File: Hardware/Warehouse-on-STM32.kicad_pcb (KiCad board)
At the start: 2 copper layers, 456.6 x 276.9 mm, 73 parts, among them J1 ESP8266, J2 Conn_01x05, J3 Barrel_Jack_Switch, J4 Conn_01x02, J5 Conn_01x02, J6 Conn_01x02, Q1 AO3400A, Q2 AO3400A, SW1 SW_Push, SW2 SW_Push, SW3 SW_Push, SW4 SW_Push, U1 STM32F103C8Tx, U10 SGP30, U11 Sensor, U2 MP2225GJ, U3 AMS1117-1.8, U4 AMS1117-2.5, U5 AMS1117-3.3, U6 DRV8820DSG, U7 DRV8820DSG, U8 DRV8820DSG, U9 AHT20, Y1 Crystal

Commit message: nm
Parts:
- removed JP1, JP2: SolderJumper_3_Open, Jumper:SolderJumper-3_P2.0mm_Open_TrianglePad1.0x1.5mm
- removed U10: SGP30, My_Sensor:SGP30
- removed U11: Sensor, My_Sensor:MEMS气体传感器
- added L2: 1.5uH, Inductor_SMD:L_Chilisin_BMRA00050520, F.Cu at (60.4, 93.4)
- added L3: 1.5uH, Inductor_SMD:L_Chilisin_BMRA00050520, F.Cu at (53.5, 93.4)
- added L4: 4.7uH, Inductor_SMD:L_Chilisin_BMRA00050520, F.Cu at (67.0, 81.4)
- added R14: 40.2K, Resistor_SMD:R_0402_1005Metric, F.Cu at (56.2, 83.2)
- added R15: 5.49K, Resistor_SMD:R_0402_1005Metric, F.Cu at (53.2, 83.2)
- added R16: 4.7K, Resistor_SMD:R_0402_1005Metric, F.Cu at (67.7, 100.5)
- added R17: 4.7K, Resistor_SMD:R_0402_1005Metric, F.Cu at (69.0, 100.5)
- added R18: 4.7K, Resistor_SMD:R_0402_1005Metric, F.Cu at (51.0, 99.2)
- added R19: 1M, Resistor_SMD:R_0402_1005Metric, F.Cu at (60.2, 104.1)
- added R20: 4.7K, Resistor_SMD:R_0402_1005Metric, F.Cu at (56.3, 99.2)
- C10, C4: value 33pF -> 10uF
- C11: value 22uF -> 220pF; footprint Capacitor_SMD:C_1206_3216Metric -> Capacitor_SMD:C_0402_1005Metric
- C12, C13: value 10uF -> 220pF; footprint Capacitor_SMD:C_0603_1608Metric -> Capacitor_SMD:C_0402_1005Metric
- C14, C18: footprint Capacitor_SMD:C_0603_1608Metric -> Capacitor_SMD:C_0402_1005Metric
- C15: value 104 -> 1uF
- C16, C8, C9: value 104 -> 10uF
- C17, C23: value 104 -> 22uF; footprint Capacitor_SMD:C_0402_1005Metric -> Capacitor_SMD:C_0805_2012Metric
- C19, C20: value 10uF -> 104; footprint Capacitor_SMD:C_0603_1608Metric -> Capacitor_SMD:C_0402_1005Metric
- C22, C7: value 104 -> 33pF
- C24, C25, C26: footprint Capacitor_SMD:CP_Elec_4x5.4 -> Capacitor_SMD:C_0201_0603Metric
- C6: value 22uF -> 104; footprint Capacitor_SMD:C_1210_3225Metric -> Capacitor_SMD:C_0402_1005Metric
- L1: value 4.7uH -> 1.5uH; footprint Inductor_SMD:L_Chilisin_BMRx00060630 -> Inductor_SMD:L_Chilisin_BMRA00050520
- R10: value 4.7K -> 200K
- R11, R13: value 4.7K -> 100K
- R12: value 1M -> 100K
- R6: value 100K -> 510K
- R7: value 40.2K -> 110K
- R8: value 5.49K -> 470K
- R9: value 4.7K -> 150K
- U2: value MP2225GJ -> EA3036C; footprint Package_TO_SOT_SMD:TSOT-23-8 -> Package_DFN_QFN:QFN-20-1EP_3x3mm_P0.4mm_EP1.65x1.65mm
- U3: value AMS1117-1.8 -> MP2225GJ; footprint Package_TO_SOT_SMD:SOT-223-3_TabPin2 -> Package_TO_SOT_SMD:TSOT-23-8
- U4: value AMS1117-2.5 -> DRV8820DSG; footprint Package_TO_SOT_SMD:SOT-223-3_TabPin2 -> Package_SON:WSON-8-1EP_2x2mm_P0.5mm_EP0.9x1.6mm
- U5: value AMS1117-3.3 -> DRV8820DSG; footprint Package_TO_SOT_SMD:SOT-223-3_TabPin2 -> Package_SON:WSON-8-1EP_2x2mm_P0.5mm_EP0.9x1.6mm
- U7: value DRV8820DSG -> AHT20; footprint Package_SON:WSON-8-1EP_2x2mm_P0.5mm_EP0.9x1.6mm -> My_Sensor:AHT20
- U8: value DRV8820DSG -> SGP30; footprint Package_SON:WSON-8-1EP_2x2mm_P0.5mm_EP0.9x1.6mm -> My_Sensor:SGP30
- U9: value AHT20 -> Sensor; footprint My_Sensor:AHT20 -> My_Sensor:MEMS气体传感器
- moved C13 214.5 mm to (52.0, 86.8)
- moved C19 210.6 mm to (59.8, 79.1)
- moved C22 204.0 mm to (54.7, 83.2), turned to 90 degrees
- moved C16 200.3 mm to (54.8, 89.3), turned to 180 degrees
- moved C10 192.5 mm to (52.0, 89.3), turned to 0 degrees
- moved L1 190.9 mm to (67.0, 93.4), turned to 90 degrees
- moved R8 190.0 mm to (54.8, 86.8), turned to 0 degrees
- moved U2 188.4 mm to (60.1, 87.4), turned to 0 degrees
- moved C9 187.2 mm to (65.7, 89.3), turned to 0 degrees
- moved C12 184.2 mm to (54.8, 88.0)
- moved C11 182.5 mm to (68.5, 86.8)
- moved C18 177.7 mm to (57.8, 83.2), turned to 90 degrees
- moved R7 177.1 mm to (68.5, 85.5), turned to 180 degrees
- moved R6 177.0 mm to (68.5, 88.0), turned to 180 degrees
- moved C8 175.8 mm to (68.5, 89.3), turned to 180 degrees
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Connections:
- C10 pad 1: Net-(U2-FB) -> +1V8
- C10 pad 2: +5V -> GND
- C11 pad 1: +5V -> +3V3
- C11 pad 2: GND -> Net-(U2-FB1)
- C12 pad 1: +5V -> +2V5
- C12 pad 2: GND -> Net-(U2-FB2)
- C13 pad 1: +5V -> +1V8
- C13 pad 2: GND -> Net-(U2-LX3)
- C17 pad 1: +5V -> +12V
- C18 pad 1: +1V8 -> +5V
- C19 pad 1: +2V5 -> +12V
- C20 pad 1: +3V3 -> GND
- C20 pad 2: GND -> Net-(U3-VCC)
- C21 pad 1: +1V8 -> Net-(U3-BST)
- C21 pad 2: GND -> Net-(U3-SW)
- C22 pad 1: +2V5 -> +5V
- C22 pad 2: GND -> Net-(U3-FB)
- C23 pad 1: +3V3 -> +5V
- C4 pad 1: Net-(U1-PD0) -> +3V3
- C5 pad 1: Net-(U1-PD1) -> Net-(U1-PD0)
- C6 pad 1: +12V -> +3V3
- C7 pad 1: +12V -> Net-(U1-PD1)
- C8 pad 1: GND -> +3V3
- C8 pad 2: Net-(U2-VCC) -> GND
- C9 pad 1: Net-(U2-SW) -> +2V5
- C9 pad 2: Net-(U2-BST) -> GND
- L1 pad 1: Net-(U2-SW) -> +3V3
- L1 pad 2: +5V -> Net-(U2-LX1)
- R10 pad 1: +3V3 -> +1V8
- R10 pad 2: /SDA -> Net-(U2-LX3)
- R11 pad 1: +1V8 -> GND
- R11 pad 2: /传感器模块/SDA1V8 -> Net-(U2-LX3)
- R12 pad 1: /ADC -> +5V
- R12 pad 2: GND -> Net-(U2-EN1)
- R13 pad 1: +1V8 -> +12V
- R13 pad 2: /传感器模块/SCL1V8 -> Net-(U3-EN/SYNC)
- R6 pad 1: +12V -> +3V3
- R6 pad 2: Net-(U2-EN/SYNC) -> Net-(U2-FB1)
- R7 pad 1: +5V -> GND
- R7 pad 2: Net-(U2-FB) -> Net-(U2-FB1)
- R8 pad 1: Net-(U2-FB) -> +2V5
- R8 pad 2: GND -> Net-(U2-FB2)
- R9 pad 1: +3V3 -> GND
- R9 pad 2: /SCL -> Net-(U2-FB2)
- U1 pad 20: /BOOT1 -> GND
- U1 pad 44: /BOOT0 -> GND
- U2 pad 2: +12V -> Net-(U2-FB3)
- U2 pad 3: Net-(U2-SW) -> Net-(U2-FB2)
- U2 pad 5: Net-(U2-BST) -> GND
- U2 pad 6: Net-(U2-EN/SYNC) -> Net-(U2-LX2)
- U2 pad 7: Net-(U2-VCC) -> +5V
- U2 pad 8: Net-(U2-FB) -> Net-(U2-EN1)
- U3 pad 2: +1V8 -> +12V
- U3 pad 3: +5V -> Net-(U3-SW)
- U4 pad 1: GND -> +12V
- U4 pad 2: +2V5 -> Net-(J4-Pin_1)
- U4 pad 3: +5V -> Net-(J4-Pin_2)
- U5 pad 1: GND -> +12V
- U5 pad 2: +3V3 -> Net-(J5-Pin_1)
- U5 pad 3: +5V -> Net-(J5-Pin_2)
- U6 pad 2: Net-(J4-Pin_1) -> Net-(J6-Pin_1)
- U6 pad 3: Net-(J4-Pin_2) -> Net-(J6-Pin_2)
- U6 pad 5: /AEN -> /CEN
- U6 pad 6: /APH -> +3V3
- U6 pad 8: /ASLEEP -> /CSLEEP
- U7 pad 1: +12V -> unconnected-(U7-NC-Pad1)
- U7 pad 2: Net-(J5-Pin_1) -> +3V3
- U7 pad 3: Net-(J5-Pin_2) -> /SCL
- U7 pad 4: GND -> /SDA
- U7 pad 5: /BEN -> GND
- U7 pad 6: +3V3 -> unconnected-(U7-NC-Pad6)
- U8 pad 1: +12V -> +1V8
- U8 pad 2: Net-(J6-Pin_1) -> GND
- U8 pad 3: Net-(J6-Pin_2) -> /传感器模块/SDA1V8
- U8 pad 5: /CEN -> +1V8
- U8 pad 6: +3V3 -> /传感器模块/SCL1V8
- U8 pad 7: +3V3 -> GND
- U9 pad 1: unconnected-(U9-NC-Pad1) -> +2V5
- U9 pad 2: +3V3 -> /ADC
- U9 pad 3: /SCL -> GND
- U9 pad 4: /SDA -> +3V3
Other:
- board size 456.6 x 276.9 mm -> 57 x 47 mm

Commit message: nm
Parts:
- J3: footprint Connector_BarrelJack:BarrelJack_CLIFF_FC681465S_SMT_Horizontal -> Connector_BarrelJack:BarrelJack_XKB_DC-044A-2.5A-2.5
- moved J3 3.98 mm to (64.7, 65.3), turned to 0 degrees
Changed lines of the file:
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@@
     )
   )
-  (footprint "Connector_BarrelJack:BarrelJack_CLIFF_FC681465S_SMT_Horizontal" (layer "F.Cu")
-    (at 65.19 69.294 -90)
-    (descr "Surface-mount DC Barrel Jack, https://www.cliffuk.co.uk/products/dcconnectors/FC681465S.pdf")
-    (tags "Power Jack SMT")
+  (footprint "Connector_BarrelJack:BarrelJack_XKB_DC-044A-2.5A-2.5" (layer "F.Cu")
+    (at 64.7 65.346)
     (property "Sheetfile" "电源模块.kicad_sch")
     (property "Sheetname" "电源模块")
@@
     (property "ki_keywords" "DC power barrel jack connector")
     (attr smd)
-    (fp_text reference "J3" (at -6.5 6.5 90) (layer "F.SilkS") hide
+    (fp_text reference "J3" (at 0 -6.096 unlocked) (layer "F.SilkS")
+        (effects (font (size 1 1) (thickness 0.1)))
+    )
+    (fp_text value "Barrel_Jack_Switch" (at 0 8.128 unlocked) (layer "F.Fab")
         (effects (font (size 1 1) (thickness 0.15)))
     )
-    (fp_text value "Barrel_Jack_Switch" (at -0.5 8.5 90) (layer "F.Fab")
+    (fp_text user "${REFERENCE}" (at -0.127 9.779 unlocked) (layer "F.Fab")
         (effects (font (size 1 1) (thickness 0.15)))
     )
-    (fp_text user "${REFERENCE}" (at -0.5 0.5 90) (layer "F.Fab")
-        (effects (font (size 1 1) (thickness 0.15)))
-    )
-    (fp_line (start -8.11 -4.56) (end -4.5 -4.56)
-      (stroke (width 0.12) (type solid)) (layer "F.SilkS"))
-    (fp_line (start -8.11 4.56) (end -8.11 -4.56)
-      (stroke (width 0.12) (type solid)) (layer "F.SilkS"))
-    (fp_line (start -8.11 4.56) (end -4.5 4.56)
-      (stroke (width 0.12) (type solid)) (layer "F.SilkS"))
-    (fp_line (start -4.8 -3) (end 0 -3)
-      (stroke (width 0.12) (type solid)) (layer "F.SilkS"))
-    (fp_line (start -4.8 3) (end 0 3)
-      (stroke (width 0.12) (type solid)) (layer "F.SilkS"))
-    (fp_line (start -4.8 4.56) (end -4.8 -4.56)
-      (stroke (width 0.12) (type solid)) (layer "F.SilkS"))
-    (fp_line (start -4.26 -7.26) (end -4.26 -5.36)
-      (stroke (width 0.12) (type solid)) (layer "F.SilkS"))
-    (fp_line (start -2.92 -7.26) (end -4.26 -7.26)
-      (stroke (width 0.12) (type solid)) (layer "F.SilkS"))
-    (fp_line (start -1.5 -4.56) (end 1.5 -4.56)
-      (stroke (width 0.12) (type solid)) (layer "F.SilkS"))
-    (fp_line (start -1.5 4.56) (end 1.5 4.56)
-      (stroke (width 0.12) (type solid)) (layer "F.SilkS"))
-    (fp_line (start 4.5 -4.56) (end 6.81 -4.56)
-      (stroke (width 0.12) (type solid)) (layer "F.SilkS"))
-    (fp_line (start 4.5 4.56) (end 6.81 4.56)
-      (stroke (width 0.12) (type solid)) (layer "F.SilkS"))
-    (fp_line (start 6.81 4.56) (end 6.81 -4.56)
-      (stroke (width 0.12) (type solid)) (layer "F.SilkS"))
-    (fp_arc (start 0 -3) (mid 3 0) (end 0 3)
-      (stroke (width 0.12) (type solid)) (layer "F.SilkS"))
-    (fp_line (start -8.5 -7.5) (end 7.2 -7.5)
-      (stroke (width 0.05) (type solid)) (layer "F.CrtYd"))
-    (fp_line (start -8.5 7.5) (end -8.5 -7.5)
-      (stroke (width 0.05) (type solid)) (layer "F.CrtYd"))
-    (fp_line (start -8.5 7.5) (end 7.2 7.5)
-      (stroke (width 0.05) (type solid)) (layer "F.CrtYd"))
-    (fp_line (start 7.2 7.5) (end 7.2 -7.5)
-      (stroke (width 0.05) (type solid)) (layer "F.CrtYd"))
-    (fp_line (start -8 -4.45) (end -4 -4.45)
-      (stroke (width 0.1) (type solid)) (layer "F.Fab"))
-    (fp_line (start -8 4.45) (end -8 -4.45)
-      (stroke (width 0.1) (type solid)) (layer "F.Fab"))
-    (fp_line (start -8 4.45) (end 6.7 4.45)
-      (stroke (width 0.1) (type solid)) (layer "F.Fab"))
-    (fp_line (start -4 -4.45) (end -3 -3.5)
-      (stroke (width 0.1) (type solid)) (layer "F.Fab"))
-    (fp_line (start -3 -3.5) (end -2 -4.45)
-      (stroke (width 0.1) (type solid)) (layer "F.Fab"))
-    (fp_line (start -2 -4.45) (end 6.7 -4.45)
-      (stroke (width 0.1) (type solid)) (layer "F.Fab"))
-    (fp_line (start 6.7 4.45) (end 6.7 -4.45)
-      (stroke (width 0.1) (type solid)) (layer "F.Fab"))
-    (pad "" np_thru_hole oval (at -2.9 0) (size 2 1.5) (drill oval 2 1.5) (layers "*.Cu" "*.Mask"))
-    (pad "" np_thru_hole circle (at 1.5 0) (size 2 2) (drill 2) (layers "*.Cu" "*.Mask"))
-    (pad "1" smd rect (at -3 -5.5) (size 3 2) (layers "F.Cu" "F.Paste" "F.Mask")
-      (net 22 "Net-(J3-Pad1)") (pintype "passive"))
-    (pad "1" smd rect (at 3 -5.5) (size 3 2) (layers "F.Cu" "F.Paste" "F.Mask")
-      (net 22 "Net-(J3-Pad1)") (pintype "passive"))
-    (pad "2" smd rect (at 3 5.5) (size 3 2) (layers "F.Cu" "F.Paste" "F.Mask")
-      (net 2 "GND") (pintype "passive"))
-    (pad "3" smd rect (at -3 5.5) (size 3 2) (layers "F.Cu" "F.Paste" "F.Mask")
-      (net 2 "GND") (pintype "passive"))
-    (model "${KICAD6_3DMODEL_DIR}/Connector_BarrelJack.3dshapes/BarrelJack_CLIFF_FC681465S_SMT_Horizontal.wrl"
-      (offset (xyz 0 0 0))
+    (fp_line (start -4.75 -5.1) (end -4.75 -3.449)
+      (stroke (width 0.1) (type default)) (layer "F.SilkS"))
+    (fp_line (start -4.75 -5.1) (end 5.25 -5.1)
+      (stroke (width 0.1) (type default)) (layer "F.SilkS"))
+    (fp_line (start -4.75 -0.782) (end -4.75 4.298)
+      (stroke (width 0.1) (type default)) (layer "F.SilkS"))
+    (fp_line (start -4.75 6.75) (end -4.75 6.584)
+      (stroke (width 0.1) (type default)) (layer "F.SilkS"))
+    (fp_line (start 5.25 -5.1) (end 5.25 -3.449)
+      (stroke (width 0.1) (type default)) (layer "F.SilkS"))
+    (fp_line (start 5.25 6.75) (end -4.75 6.75)
+      (stroke (width 0.1) (type default)) (layer "F.SilkS"))
+    (fp_line (start 5.25 6.75) (end 5.25 -0.782)
+      (stroke (width 0.1) (type default)) (layer "F.SilkS"))
+    (fp_rect (start -2 -2) (end 0 0)
+      (stroke (width 0.1) (type default)) (fill none) (layer "Edge.Cuts"))
+    (pad "2" thru_hole oval (at 3.95 5.4 90) (size 2 1.1) (drill oval 1.6 0.8) (layers "*.Cu" "*.Mask")
+      (net 2 "GND") (pintype "passive") (solder_mask_margin 0.04) (thermal_bridge_angle 45))
+    (pad "3" thru_hole oval (at -1.25 5.4 90) (size 2 1.1) (drill oval 1.6 0.8) (layers "*.Cu" "*.Mask")
+      (net 2 "GND") (pintype "passive") (solder_mask_margin 0.04) (thermal_bridge_angle 45))
+    (pad "4" thru_hole oval (at -4.65 5.4 90) (size 2 1.1) (drill oval 1.6 0.8) (layers "*.Cu" "*.Mask")
+      (solder_mask_margin 0.04) (thermal_bridge_angle 45))
+    (pad "5" thru_hole oval (at -4.65 -2.1 90) (size 2.4 0.8) (drill oval 2 0.5) (layers "*.Cu" "*.Mask")
+      (solder_mask_margin 0.04) (thermal_bridge_angle 45))
+    (pad "5" thru_hole oval (at 5.15 -2.1 90) (size 2.4 0.8) (drill oval 2 0.5) (layers "*.Cu" "*.Mask")
+      (solder_mask_margin 0.04) (thermal_bridge_angle 45))
+    (model "${KICAD7_3DMODEL_DIR}/Connector_BarrelJack.3dshapes/BarellJack_XKB_DC-044A-2.5A-2.5.stp"
+      (offset (xyz 0.2 4.9 4))
       (scale (xyz 1 1 1))
-      (rotate (xyz 0 0 0))
+      (rotate (xyz 90 180 0))
     )
   )

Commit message: 完成布局
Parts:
- C1: footprint Capacitor_SMD:C_0603_1608Metric -> Capacitor_SMD:C_0402_1005Metric
- J2: footprint Connector_PinHeader_2.54mm:PinHeader_1x05_P2.54mm_Vertical -> Connector_PinHeader_1.00mm:PinHeader_1x05_P1.00mm_Vertical
- J3: value Barrel_Jack_Switch -> Barrel_Jack_Switch_MountingPin
- L1, L2, L3, L4: footprint Inductor_SMD:L_Chilisin_BMRA00050520 -> Inductor_SMD:L_1206_3216Metric
- SW1, SW2, SW3, SW4: footprint Button_Switch_SMD:SW_Tactile_SPST_NO_Straight_CK_PTS636Sx25SMTRLFS -> Button_Switch_SMD:SW_XKB_TS-1185-B-A-B-A
- SW5: footprint Library:SW -> Button_Switch_THT:SW_XKB_SS-12D10L5
- U7: footprint My_Sensor:AHT20 -> Sensor:AHT20
- U8: footprint My_Sensor:SGP30 -> Sensor:SGP30
- U9: footprint My_Sensor:MEMS气体传感器 -> Sensor:MEMS气体传感器
- Y1: value Crystal -> 8MHz; footprint Crystal:Crystal_SMD_5032-2Pin_5.0x3.2mm -> Crystal:Crystal_SMD_3225-4Pin_3.2x2.5mm
- moved SW5 75.8 mm to (119.4, 104.5), turned to 0 degrees
- moved R13 74.7 mm to (125.4, 112.7), turned to -90 degrees
- moved C20 74.6 mm to (119.4, 114.5), turned to 0 degrees
- moved C22 73.8 mm to (121.6, 114.5), turned to 180 degrees
- moved R15 73.8 mm to (119.4, 115.9), turned to 180 degrees
- moved R14 73.1 mm to (121.6, 115.9), turned to 180 degrees
- moved C19 72.7 mm to (125.4, 110.5), turned to 90 degrees
- moved U3 72.6 mm to (120.2, 111.5), turned to -90 degrees
- moved C21 71.9 mm to (116.8, 111.4)
- moved C17 69.8 mm to (123.4, 111.3), turned to -90 degrees
- moved Q2 67.5 mm to (113.2, 131.7)
- moved J2 66.1 mm to (149.8, 132.8), turned to -90 degrees
- moved C24 65.9 mm to (133.4, 110.6)
- moved C27 65.9 mm to (132.2, 110.8)
- moved C25 65.6 mm to (142.4, 110.6)
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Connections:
- C13 pad 2: Net-(U2-LX3) -> Net-(U2-FB3)
- J2 pad 1: /SWDIO -> /SWCLK
- J2 pad 2: /SWCLK -> /SWDIO
- J2 pad 4: /USART1_TX -> /USART1_RX
- J2 pad 5: /USART1_RX -> /USART1_TX
- L3 pad 2: Net-(U2-FB3) -> Net-(U2-LX3)
- R10 pad 2: Net-(U2-LX3) -> Net-(U2-FB3)
- R11 pad 2: Net-(U2-LX3) -> Net-(U2-FB3)
- U1 pad 14: unconnected-(U1-PA4-Pad14) -> /KEY2
- U1 pad 15: unconnected-(U1-PA5-Pad15) -> /KEY1
- U1 pad 16: /ASLEEP -> /KEY0
- U1 pad 17: /APH -> unconnected-(U1-PA7-Pad17)
- U1 pad 2: /KEY0 -> /ASLEEP
- U1 pad 21: /USART1_RX -> unconnected-(U1-PB10-Pad21)
- U1 pad 29: /AEN -> unconnected-(U1-PA8-Pad29)
- U1 pad 3: /KEY1 -> /APH
- U1 pad 30: /BSLEEP -> /USART1_TX
- U1 pad 31: /BEN -> /USART1_RX
- U1 pad 32: /CSLEEP -> unconnected-(U1-PA11-Pad32)
- U1 pad 33: /CEN -> unconnected-(U1-PA12-Pad33)
- U1 pad 38: unconnected-(U1-PA15-Pad38) -> /CSLEEP
- U1 pad 39: unconnected-(U1-PB3-Pad39) -> /CEN
- U1 pad 4: /KEY2 -> /AEN
- U1 pad 40: unconnected-(U1-PB4-Pad40) -> /BSLEEP
- U1 pad 41: unconnected-(U1-PB5-Pad41) -> /BEN
- U1 pad 46: /USART1_TX -> unconnected-(U1-PB9-Pad46)
- Y1 pad 2: Net-(U1-PD1) -> GND
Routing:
- added copper zone on F.Cu, net +12V
- added copper zone on B.Cu, net Net-(J3-Pad1)
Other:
- board size 57 x 47 mm -> 53 x 35 mm

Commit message: 完成部分布线
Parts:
- moved C18 0.80 mm to (107.8, 114.4)
- moved R12 0.40 mm to (109.6, 114.4)
- turned C19 to -90 degrees
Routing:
- net +1V8: track 0.00 -> 23.7 mm
- net +12V: track 0.00 -> 23.4 mm, vias 0 -> 12
- net +5V: track 0.00 -> 21.3 mm, vias 0 -> 6
- net Net-(U3-SW): track 0.00 -> 11.4 mm
- net Net-(U2-FB2): track 0.00 -> 10.9 mm
- net Net-(U2-FB1): track 0.00 -> 10.5 mm
- net Net-(U2-LX3): track 0.00 -> 10.0 mm
- net Net-(U2-EN1): track 0.00 -> 9.32 mm, vias 0 -> 2
- net Net-(U3-EN/SYNC): track 0.00 -> 6.73 mm, vias 0 -> 2
- net Net-(U2-FB3): track 0.00 -> 6.52 mm
- net Net-(J6-Pin_1): track 0.00 -> 5.97 mm
- net Net-(J5-Pin_1): track 0.00 -> 5.97 mm
- net Net-(J4-Pin_1): track 0.00 -> 5.97 mm
- net +3V3: track 0.00 -> 5.41 mm
- net +2V5: track 0.00 -> 5.41 mm
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- added copper zone on B.Cu, net +12V
- added copper zone on B.Cu, net +5V
- removed copper zone on F.Cu, net +12V

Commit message: 绘制第一版
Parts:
- moved R16 0.10 mm to (108.2, 126.9)
- moved R17 0.10 mm to (113.0, 126.9)
- moved C1 0.09 mm to (149.1, 114.6)
- moved R1 0.09 mm to (149.1, 115.8)
- turned R20 to 0 degrees
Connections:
- U1 pad 21: unconnected-(U1-PB10-Pad21) -> /SCL
- U1 pad 22: unconnected-(U1-PB11-Pad22) -> /SDA
- U1 pad 42: /SCL -> unconnected-(U1-PB6-Pad42)
- U1 pad 43: /SDA -> unconnected-(U1-PB7-Pad43)
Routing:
- net +3V3: track 5.41 -> 127.6 mm, vias 0 -> 14
- net /SCL: track 0.00 -> 38.3 mm, vias 0 -> 3
- net /SDA: track 0.00 -> 34.8 mm, vias 0 -> 4
- net /SWCLK: track 0.00 -> 24.2 mm
- net /ESP_TX: track 0.00 -> 23.3 mm, vias 0 -> 1
- net /ADC: track 0.00 -> 22.8 mm, vias 0 -> 4
- net /SWDIO: track 0.00 -> 19.6 mm
- net /ESP_RX: track 0.00 -> 19.5 mm, vias 0 -> 1
- net /USART1_RX: track 0.00 -> 17.2 mm
- net /USART1_TX: track 0.00 -> 16.2 mm
- net +1V8: track 23.7 -> 39.8 mm, vias 0 -> 2
- net +2V5: track 5.41 -> 21.3 mm
- net /CSLEEP: track 0.00 -> 14.0 mm
- net /传感器模块/SDA1V8: track 0.00 -> 13.6 mm, vias 0 -> 4
- net /CEN: track 0.00 -> 13.1 mm
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- added copper zone on B.Cu, net GND
- added copper zone on F.Cu, net GND

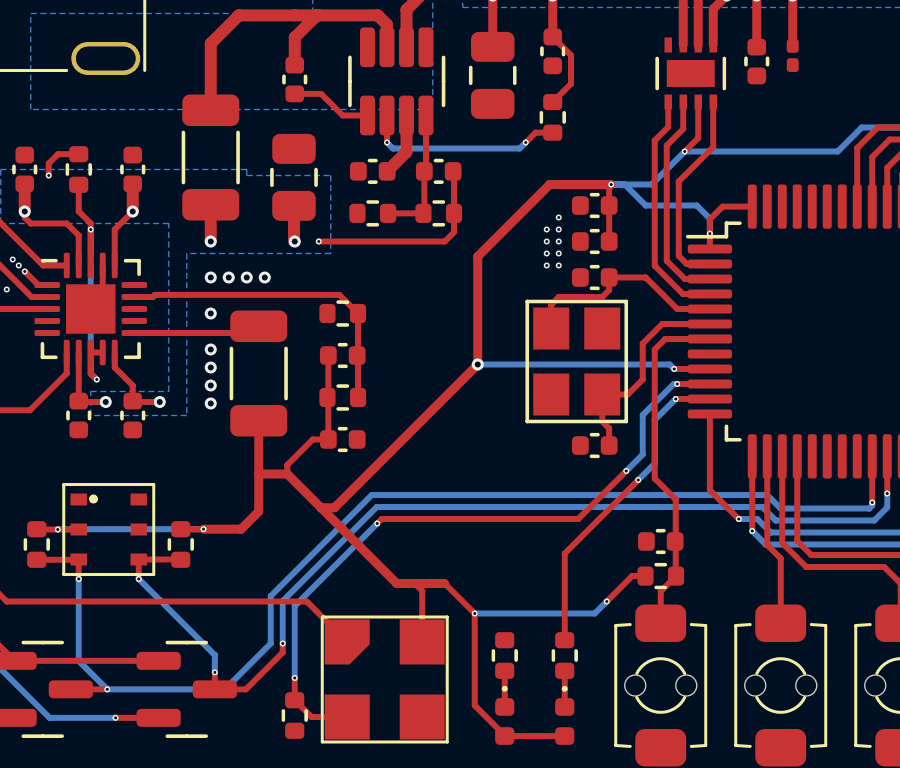
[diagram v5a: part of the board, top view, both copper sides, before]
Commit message: 修改了电机驱动芯片旁的电容封装为0603
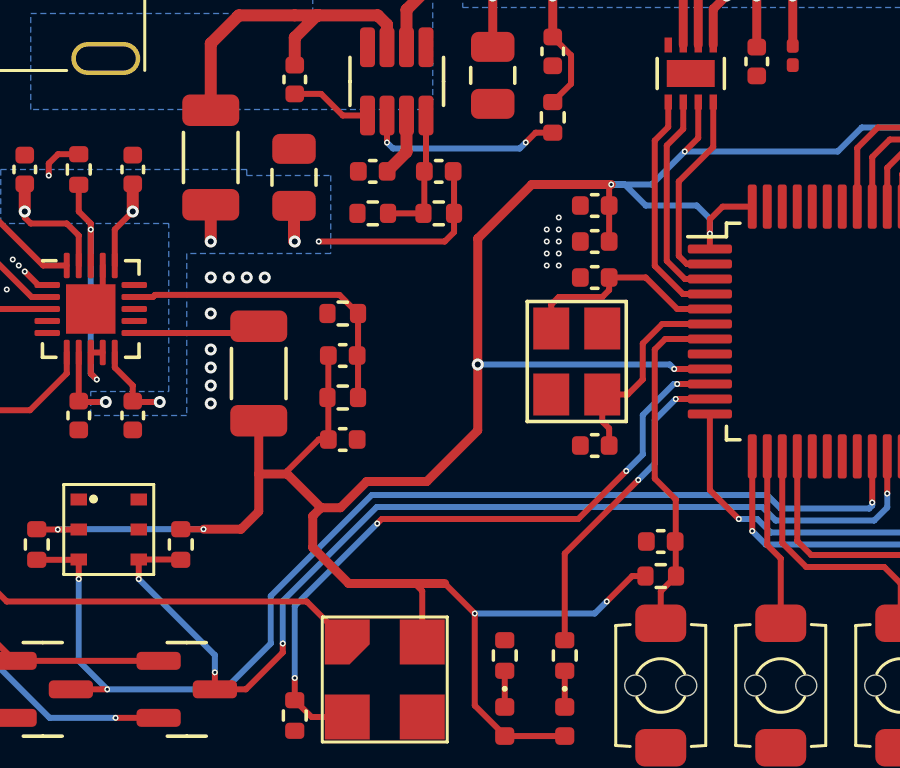
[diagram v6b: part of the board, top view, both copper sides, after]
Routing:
- net +3V3: track 127.6 -> 130.3 mm

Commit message: coding
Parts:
- added J3: UART, Connector_Yource:1.25-3A, F.Cu at (145.0, 120.2)
- C24, C25, C26: footprint Capacitor_SMD:C_0201_0603Metric -> Capacitor_SMD:C_0603_1608Metric
- J2: value Conn_01x05 -> SWD; footprint Connector_PinHeader_1.00mm:PinHeader_1x05_P1.00mm_Vertical -> Connector_Yource:1.25-5A
- moved J2 2.68 mm to (147.4, 131.6), turned to 0 degrees
- moved C24 0.28 mm to (133.6, 110.8)
- moved C25 0.28 mm to (142.6, 110.8)
- moved C26 0.28 mm to (151.6, 110.8)
- renumbered J3 to J4, J4 to J5, J5 to J6, J6 to J7
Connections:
- C3 pad 1: /RESET -> /NRST
- J2 pad 1: /SWCLK -> +3V3
- J2 pad 4: /USART1_RX -> /SWCLK
- J2 pad 5: /USART1_TX -> /NRST
- R5 pad 2: /RESET -> /NRST
- SW4 pad 2: /RESET -> /NRST
- U1 pad 7: /RESET -> /NRST
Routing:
- net /NRST: track 0.00 -> 33.5 mm, vias 0 -> 1
- net /RESET: track 11.6 -> 0.00 mm
- net /USART1_RX: track 17.2 -> 6.31 mm, vias 0 -> 1
- net +3V3: track 130.3 -> 140.7 mm, vias 14 -> 15
- net /USART1_TX: track 16.2 -> 6.62 mm, vias 0 -> 1
- net /SWDIO: track 19.6 -> 17.6 mm
- net /SWCLK: track 24.2 -> 22.5 mm
- net +12V: track 26.0 -> 25.5 mm
- net GND: vias 31 -> 37
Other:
- board text added: "SWD"
- board text added: "UART"
